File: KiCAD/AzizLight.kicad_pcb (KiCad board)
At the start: 2 copper layers, 70.1 x 29.2 mm, 58 parts, among them P1 +9V, Q1 BS170, Q2 BS170, Q3 BS170, Q4 BS170, SW1 Reset, SW2 Trigger Out, U1 MCP602, U2 LM393, U3 MCP601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

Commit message: v1.3 commit
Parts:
- removed C13: 0.1uF, Capacitors_SMD:C_0805_HandSoldering
- removed D2, D3, D4, D5, D6: 1N4148, Diodes_SMD:SOD-523
- removed R8: 100, Resistors_SMD:R_0805_HandSoldering
- removed U3: MCP601, SMD_Packages:SOIC-8-N
- added P2: Trigger Out, TO_SOT_Packages_SMD:TO-252-2Lead, F.Cu at (181.1, 88.1)
- added Q5: BS170, TO_SOT_Packages_SMD:SOT-23, F.Cu at (178.2, 92.3)
- added R26: 100, Resistors_SMD:R_0805_HandSoldering, F.Cu at (173.8, 91.1)
- added R27: 1M, Resistors_SMD:R_0805_HandSoldering, F.Cu at (173.8, 93.3)
- C11: value 0.1uF -> 0.33uF
- C12: value 0.33uF -> 0.1uF
- C4: value 0.1uF -> 100uF; footprint Capacitors_SMD:C_0805_HandSoldering -> Capacitors_SMD:c_elec_6.3x5.8
- C6: value 0.1uF -> 10uF
- C8: value 10uF -> 100pF
- C9: value 100pF -> 0.1uF
- R1: value 68k -> 10k
- R14: value 10k -> 120k
- R15: value 120k -> 10M
- R16: value 10M -> 560k
- R19: value 560k -> 10k
- R20: value 10k -> 12k
- R21: value 12k -> 10k
- R24: value 10k -> 1M
- R25: value 1M -> 4.7k
- R5: value 10k -> 100
- R6: value 100 -> 100k
- R7: value 100k -> 10k
- SW2: value Trigger Out -> Invert; footprint Capacitors_SMD:C_2225_HandSoldering -> TO_SOT_Packages_SMD:TO-252-2Lead
- moved SW1 51.9 mm to (122.3, 97.8), turned to 270 degrees
- moved C8 36.7 mm to (134.3, 85.4), turned to 270 degrees
- moved C12 34.4 mm to (182.4, 96.5)
- moved Q3 32.5 mm to (151.9, 80.0), turned to 270 degrees
- moved U4 31.9 mm to (173.9, 101.6), turned to 270 degrees
- moved C11 28.8 mm to (174.0, 96.5), turned to 180 degrees
- moved Q1 28.6 mm to (160.0, 79.9), turned to 270 degrees
- moved Q4 27.2 mm to (150.9, 83.5), turned to 0 degrees
- moved Q2 26.9 mm to (156.0, 80.0), turned to 0 degrees
- moved R16 26.8 mm to (136.8, 85.5), turned to 270 degrees
- moved R22 26.4 mm to (151.7, 101.5), turned to 180 degrees
- moved C6 26.3 mm to (151.6, 90.9), turned to 0 degrees
- moved R5 26.0 mm to (143.8, 92.3), turned to 270 degrees
- moved R20 25.5 mm to (151.7, 104.1), turned to 180 degrees
- moved R24 25.3 mm to (163.0, 86.8), turned to 90 degrees
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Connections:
- C12 pad 1: Net-(C12-Pad1) -> +5V
- C4 pad 1: GND -> +5V
- C4 pad 2: Net-(C4-Pad2) -> GND
- C8 pad 2: GND -> Net-(C5-Pad1)
- C9 pad 2: Net-(C5-Pad1) -> GND
- D1 pad 1: Net-(C9-Pad1) -> Net-(C6-Pad1)
- L1 pad 2: Net-(C12-Pad1) -> Net-(C11-Pad1)
- Q1 pad 1: Net-(C8-Pad1) -> Net-(Q1-Pad1)
- Q2 pad 1: Net-(Q1-Pad3) -> Net-(C7-Pad1)
- Q2 pad 3: Net-(Q2-Pad3) -> Net-(Q1-Pad1)
- Q3 pad 1: Net-(Q1-Pad3) -> Net-(Q1-Pad1)
- Q3 pad 3: Net-(C8-Pad1) -> Net-(C7-Pad1)
- Q4 pad 1: Net-(D2-Pad2) -> Net-(D1-Pad2)
- R1 pad 1: Net-(D2-Pad2) -> Net-(D1-Pad2)
- R10 pad 1: Net-(C8-Pad1) -> Net-(C7-Pad1)
- R12 pad 2: Net-(Q1-Pad3) -> Net-(Q1-Pad1)
- R13 pad 1: Net-(C6-Pad1) -> Net-(R13-Pad1)
- R13 pad 2: Net-(C9-Pad1) -> Net-(C8-Pad1)
- R14 pad 1: Net-(R14-Pad1) -> Net-(R10-Pad2)
- R15 pad 1: Net-(R10-Pad2) -> Net-(R15-Pad1)
- R15 pad 2: Net-(R15-Pad2) -> Net-(C6-Pad1)
- R16 pad 1: Net-(R16-Pad1) -> Net-(C8-Pad1)
- R16 pad 2: Net-(C7-Pad1) -> Net-(C5-Pad1)
- R17 pad 2: Net-(Q1-Pad3) -> Net-(Q1-Pad1)
- R18 pad 2: Net-(R16-Pad1) -> Net-(R15-Pad1)
- R19 pad 1: Net-(C9-Pad1) -> Net-(R19-Pad1)
- R19 pad 2: Net-(C5-Pad1) -> +5V
- R2 pad 1: Net-(D2-Pad2) -> Net-(D1-Pad2)
- R2 pad 2: Net-(R14-Pad1) -> Net-(R13-Pad1)
- R20 pad 1: Net-(R20-Pad1) -> +5V
- R20 pad 2: +5V -> Net-(C9-Pad1)
- R21 pad 1: +5V -> Net-(R21-Pad1)
- R21 pad 2: Net-(C10-Pad1) -> Net-(R21-Pad2)
- R22 pad 1: Net-(R22-Pad1) -> GND
- R22 pad 2: Net-(R22-Pad2) -> Net-(C9-Pad1)
- R23 pad 2: Net-(C10-Pad1) -> Net-(R21-Pad1)
- R24 pad 2: Net-(R22-Pad1) -> Net-(Q1-Pad1)
- R25 pad 1: GND -> +5V
- R25 pad 2: Net-(Q1-Pad3) -> Net-(P2-Pad2)
- R5 pad 1: Net-(C1-Pad1) -> +5V
- R5 pad 2: GND -> Net-(C3-Pad2)
- R6 pad 2: Net-(C3-Pad2) -> Net-(C7-Pad1)
- R7 pad 1: +5V -> Net-(C1-Pad1)
- R7 pad 2: Net-(C8-Pad1) -> GND
- R9 pad 2: Net-(Q2-Pad3) -> Net-(Q1-Pad3)
- RV1 pad 1: Net-(R20-Pad1) -> Net-(R19-Pad1)
- RV1 pad 2: Net-(C11-Pad1) -> Net-(C10-Pad1)
- RV1 pad 3: Net-(R22-Pad2) -> Net-(R21-Pad2)
- SW1 pad 2: Net-(C7-Pad1) -> Net-(C6-Pad1)
- SW2 pad 1: Net-(Q2-Pad3) -> Net-(R17-Pad1)
- SW2 pad 2: Net-(R17-Pad1) -> Net-(R26-Pad2)
- U1 pad 1: Net-(D1-Pad2) -> Net-(C8-Pad1)
- U2 pad 1: Net-(D2-Pad2) -> Net-(D1-Pad2)
- U2 pad 2: Net-(C11-Pad1) -> Net-(C10-Pad1)
- U2 pad 3: Net-(R14-Pad1) -> Net-(R13-Pad1)
- U2 pad 6: Net-(C10-Pad1) -> Net-(C9-Pad1)
- U2 pad 7: Net-(C8-Pad1) -> Net-(C7-Pad1)
- U4 pad 1: Net-(C12-Pad1) -> Net-(C11-Pad1)
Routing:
- net Net-(D2-Pad2): track 63.0 -> 0.00 mm
- net Net-(C8-Pad1): track 45.1 -> 13.6 mm
- net Net-(C6-Pad1): track 14.4 -> 45.3 mm, vias 0 -> 2
- net Net-(D1-Pad2): track 5.11 -> 31.8 mm
- net Net-(Q2-Pad3): track 23.0 -> 0.00 mm
- net Net-(Q1-Pad1): track 0.00 -> 22.5 mm
- net Net-(C5-Pad1): track 25.1 -> 8.87 mm
- net Net-(P2-Pad2): track 0.00 -> 12.6 mm
- net Net-(R15-Pad2): track 10.2 -> 0.00 mm
- net Net-(C12-Pad1): track 9.71 -> 0.00 mm
- net Net-(R13-Pad1): track 0.00 -> 9.49 mm
- net Net-(R14-Pad1): track 8.89 -> 0.00 mm
- net Net-(C4-Pad2): track 7.37 -> 0.00 mm
- net Net-(C7-Pad1): track 36.3 -> 29.0 mm
- net Net-(C11-Pad1): track 13.5 -> 7.02 mm
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
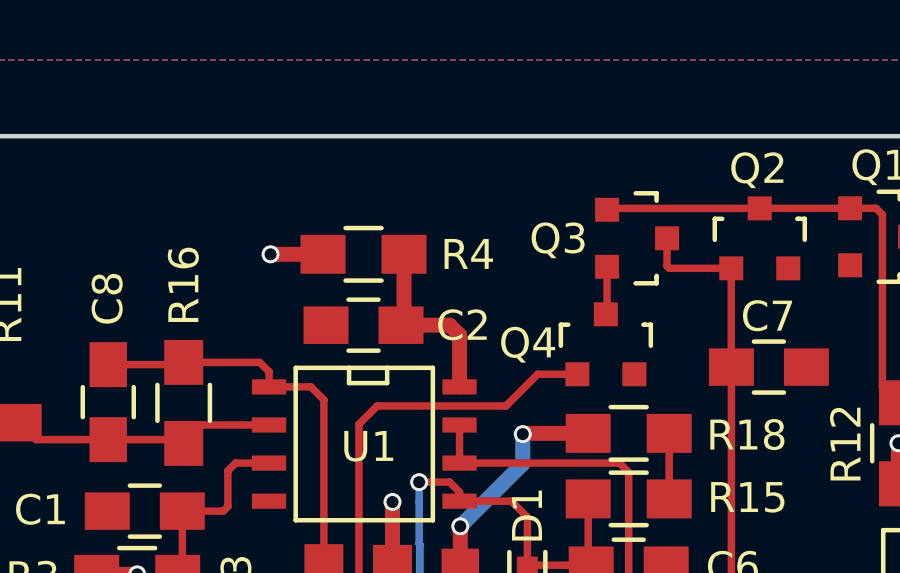
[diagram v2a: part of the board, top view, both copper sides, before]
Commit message: Added pull down resistor R28
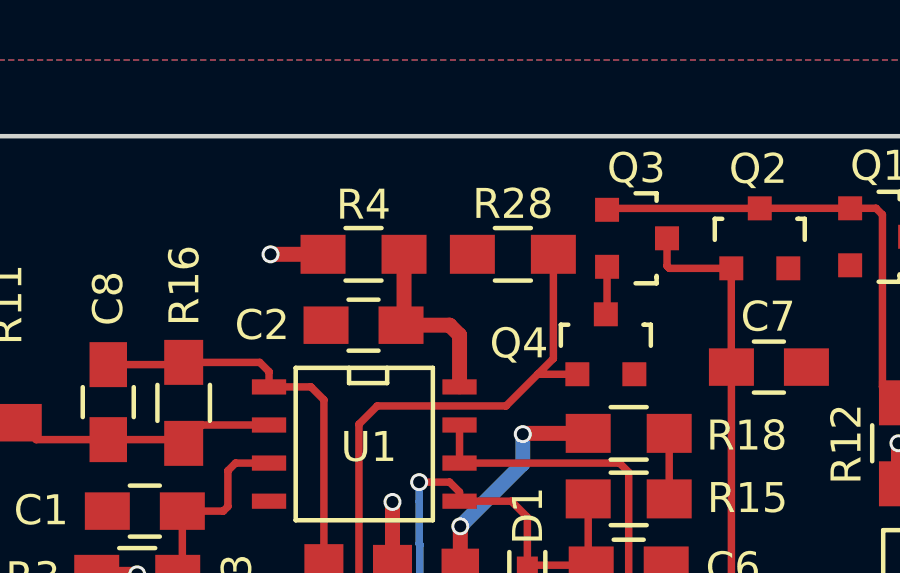
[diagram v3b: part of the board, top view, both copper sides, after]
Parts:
- added R28: 1M, Resistors_SMD:R_0805_HandSoldering, F.Cu at (147.8, 80.5)
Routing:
- net Net-(D1-Pad2): track 31.8 -> 36.0 mm
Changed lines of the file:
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@@
 (kicad_pcb (version 4) (host pcbnew 4.0.4-stable)
   (general
-    (links 100)
+    (links 102)
     (no_connects 0)
     (area 111.76 74.041 187.960001 109.601001)
     (thickness 1.6)
     (drawings 20)
-    (tracks 199)
+    (tracks 201)
     (zones 0)
-    (modules 54)
+    (modules 55)
     (nets 30)
   )
@@
     (tags "capacitor 0805")
     (attr smd)
-    (fp_text reference C2 (at 3.3274 0.0254) (layer F.SilkS)
+    (fp_text reference C2 (at -3.3782 0) (layer F.SilkS)
       (effects (font (size 1 1) (thickness 0.15)))
     )
@@
     (tags SOT-23)
     (attr smd)
-    (fp_text reference Q3 (at 0.0254 2.6162 360) (layer F.SilkS)
+    (fp_text reference Q3 (at -2.3368 0.0254 360) (layer F.SilkS)
       (effects (font (size 1 1) (thickness 0.15)))
     )
@@
     (tags SOT-23)
     (attr smd)
-    (fp_text reference Q4 (at -2.5908 -0.0254 180) (layer F.SilkS)
+    (fp_text reference Q4 (at -2.8956 -0.0254 180) (layer F.SilkS)
       (effects (font (size 1 1) (thickness 0.15)))
     )
@@
     (tags "resistor 0805")
     (attr smd)
-    (fp_text reference R4 (at 3.4798 0.0254) (layer F.SilkS)
+    (fp_text reference R4 (at 0 -1.651) (layer F.SilkS)
       (effects (font (size 1 1) (thickness 0.15)))
     )
@@
       (net 13 +5V))
     (model TO_SOT_Packages_SMD.3dshapes/TO-252-2Lead.wrl
+      (at (xyz 0 0 0))
+      (scale (xyz 1 1 1))
+      (rotate (xyz 0 0 0))
+    )
+  )
+  (module Resistors_SMD:R_0805_HandSoldering (layer F.Cu)
+    (at 147.7772 80.518)
+    (descr "Resistor SMD 0805, hand soldering")
+    (tags "resistor 0805")
+    (attr smd)
+    (fp_text reference R28 (at 0 -1.6764) (layer F.SilkS)
+      (effects (font (size 1 1) (thickness 0.15)))
+    )
+    (fp_text value 1M (at 0 2.1) (layer F.Fab)
+      (effects (font (size 1 1) (thickness 0.15)))
+    )
+    (fp_line (start -2.4 -1) (end 2.4 -1) (layer F.CrtYd) (width 0.05))
+    (fp_line (start -2.4 1) (end 2.4 1) (layer F.CrtYd) (width 0.05))
+    (fp_line (start -2.4 -1) (end -2.4 1) (layer F.CrtYd) (width 0.05))
+    (fp_line (start 2.4 -1) (end 2.4 1) (layer F.CrtYd) (width 0.05))
+    (fp_line (start 0.6 0.875) (end -0.6 0.875) (layer F.SilkS) (width 0.15))
+    (fp_line (start -0.6 -0.875) (end 0.6 -0.875) (layer F.SilkS) (width 0.15))
+    (pad 1 smd rect (at -1.35 0) (size 1.5 1.3) (layers F.Cu F.Paste F.Mask)
+      (net 2 GND))
+    (pad 2 smd rect (at 1.35 0) (size 1.5 1.3) (layers F.Cu F.Paste F.Mask)
+      (net 14 "Net-(D1-Pad2)"))
+    (model Resistors_SMD.3dshapes/R_0805_HandSoldering.wrl
       (at (xyz 0 0 0))
       (scale (xyz 1 1 1))
@@
   (via (at 181.2036 92.6592) (size 0.6) (drill 0.4) (layers F.Cu B.Cu) (net 13))
   (segment (start 181.0728 94.0562) (end 181.0512 94.0346) (width 0.25) (layer F.Cu) (net 13))
+  (segment (start 149.1272 80.518) (end 149.1272 83.994) (width 0.25) (layer F.Cu) (net 14) (status 400000))
+  (segment (start 149.1272 83.994) (end 148.60524 84.51596) (width 0.25) (layer F.Cu) (net 14))
   (segment (start 149.926 84.51596) (end 148.60524 84.51596) (width 0.25) (layer F.Cu) (net 14))
   (segment (start 142.6464 86.1822) (end 142.6464 92.2924) (width 0.25) (layer F.Cu) (net 14))
